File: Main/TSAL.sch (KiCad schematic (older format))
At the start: 39 parts, among them J1 Mini-SPOX, J2 Mini-SPOX, J3 Mini-Fit_Jr, J4 Mini-SPOX, J5 Mini-SPOX, Q1 IRLML2502, Q2 IRLML2502, Q3 IRLML2502, Q4 IRLML2502, U1 74HC08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

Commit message: Main board: Rev B schematics design
major redesign of power delivery and backup
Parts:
- removed C1, C4: 10u, Capacitor_SMD:C_0805_2012Metric_Pad1.15x1.40mm_HandSolder, symbol Device:C
- removed F1: 1A, Fuse:Fuseholder_Cylinder-5x20mm_Schurter_0031_8201_Horizontal_Open, symbol Device:Fuse
- removed R4: 1k, Resistor_SMD:R_0805_2012Metric_Pad1.15x1.40mm_HandSolder, symbol Device:R
- removed TP1: TP_Timer_En, TestPoint:TestPoint_THTPad_D2.0mm_Drill1.0mm, symbol Connector:TestPoint
- removed TP2: TP_RLED_Ctrl, TestPoint:TestPoint_THTPad_D2.0mm_Drill1.0mm, symbol Connector:TestPoint
- removed U3: TLV70033, Package_TO_SOT_SMD:SOT-23-5_HandSoldering, symbol Regulator_Linear:TLV70033_SOT23-5
- added Q5: IRLML2502, Package_TO_SOT_SMD:SOT-23, symbol Device:Q_NMOS_GSD
- C1: renamed from C2; value 100n -> 0.1uF; footprint Capacitor_SMD:C_0805_2012Metric_Pad1.15x1.40mm_HandSolder -> Capacitor_SMD:C_0402_1005Metric; Part CL21B104KACNNNC -> (none)
- C2: renamed from C3; value 100n -> 0.1uF; footprint Capacitor_SMD:C_0805_2012Metric_Pad1.15x1.40mm_HandSolder -> Capacitor_SMD:C_0402_1005Metric; Part CL21B104KACNNNC -> (none)
- C3: renamed from C5; value 100n -> 0.1uF; footprint Capacitor_SMD:C_0805_2012Metric_Pad1.15x1.40mm_HandSolder -> Capacitor_SMD:C_0402_1005Metric; symbol Device:C -> Device:C_Small; Part CL21B104KACNNNC -> (none)
- C4: renamed from C6; value 100n -> 0.1uF; footprint Capacitor_SMD:C_0805_2012Metric_Pad1.15x1.40mm_HandSolder -> Capacitor_SMD:C_0402_1005Metric; Part CL21B104KACNNNC -> (none)
- C5: renamed from C7; value 2.2u -> 2.2uF; footprint Capacitor_SMD:C_0805_2012Metric_Pad1.15x1.40mm_HandSolder -> Capacitor_SMD:C_0805_2012Metric; symbol Device:C -> Device:C_Small
- J1: renamed from J3; value Mini-Fit_Jr -> Micro-Fit; footprint Connector_Molex:Molex_Mini-Fit_Jr_5566-02A_2x01_P4.20mm_Vertical -> Connector_Molex:Molex_Micro-Fit_3.0_43045-0412_2x02_P3.00mm_Vertical; symbol Connector_Generic:Conn_01x02 -> Connector_Generic:Conn_02x02_Odd_Even; Part 39-28-1023 -> 43045-0413
- Q1: footprint Package_TO_SOT_SMD:SOT-23_Handsoldering -> Package_TO_SOT_SMD:SOT-23
- Q2: renamed from Q4; footprint Package_TO_SOT_SMD:SOT-23_Handsoldering -> Package_TO_SOT_SMD:SOT-23
- Q3: renamed from Q2; footprint Package_TO_SOT_SMD:SOT-23_Handsoldering -> Package_TO_SOT_SMD:SOT-23
- Q4: renamed from Q3; footprint Package_TO_SOT_SMD:SOT-23_Handsoldering -> Package_TO_SOT_SMD:SOT-23
- R1: footprint Resistor_SMD:R_0805_2012Metric_Pad1.15x1.40mm_HandSolder -> Resistor_SMD:R_0402_1005Metric; Part RC0805FR-07100KL -> (none)
- R10: renamed from R16; footprint Resistor_SMD:R_0805_2012Metric_Pad1.15x1.40mm_HandSolder -> Resistor_SMD:R_0402_1005Metric; Part RC0805FR-07100KL -> (none)
- R11: renamed from R15; footprint Resistor_SMD:R_0805_2012Metric_Pad1.15x1.40mm_HandSolder -> Resistor_SMD:R_0402_1005Metric; Part RC0805FR-07100KL -> (none)
- R2: renamed from R7; footprint Resistor_SMD:R_0805_2012Metric_Pad1.15x1.40mm_HandSolder -> Resistor_SMD:R_0402_1005Metric; symbol Device:R -> Device:R_Small; Part RC0805FR-07100KL -> (none)
- R3: renamed from R5; value 22k -> 10k; footprint Resistor_SMD:R_0805_2012Metric_Pad1.15x1.40mm_HandSolder -> Resistor_SMD:R_0805_2012Metric; symbol Device:R -> Device:R_Small; Part RC0805FR-0722KL -> (none)
- R4: renamed from R3; value 22k -> 10k; footprint Resistor_SMD:R_0805_2012Metric_Pad1.15x1.40mm_HandSolder -> Resistor_SMD:R_0402_1005Metric; symbol Device:R -> Device:R_Small; Part RC0805FR-0722KL -> (none)
- R5: renamed from R6; footprint Resistor_SMD:R_0805_2012Metric_Pad1.15x1.40mm_HandSolder -> Resistor_SMD:R_0805_2012Metric; symbol Device:R -> Device:R_Small; Part RC0805FR-07100KL -> (none)
- R6: renamed from R2; footprint Resistor_SMD:R_0805_2012Metric_Pad1.15x1.40mm_HandSolder -> Resistor_SMD:R_0402_1005Metric; Part RC0805FR-07100KL -> (none)
- R7: renamed from R19; footprint Resistor_SMD:R_0805_2012Metric_Pad1.15x1.40mm_HandSolder -> Resistor_SMD:R_0402_1005Metric; Part RC0805FR-07100KL -> (none)
- R8: renamed from R18; footprint Resistor_SMD:R_0805_2012Metric_Pad1.15x1.40mm_HandSolder -> Resistor_SMD:R_0402_1005Metric; Part RC0805FR-07100KL -> (none)
- R9: renamed from R17; footprint Resistor_SMD:R_0805_2012Metric_Pad1.15x1.40mm_HandSolder -> Resistor_SMD:R_0402_1005Metric; Part RC0805FR-07100KL -> (none)
- U1, U2: footprint Package_SO:SOIC-14_3.9x8.7mm_P1.27mm -> Package_SO:TSSOP-14_4.4x5mm_P0.65mm; Part SN74HC08DR -> SN74HC08PW
- U3: renamed from U4; footprint Package_SO:SOIC-8_3.9x4.9mm_P1.27mm -> Package_SO:TSSOP-8_3x3mm_P0.65mm; Part LMC555CMX -> LMC555CMM
- renumbered J1 to J2, J4 to J3, J2 to J4
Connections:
- net labels added: Dash_LED-, GNDPWR
- net labels removed: +2V5, TS_Inact_Out, VCC_F
- wire segments 91 -> 110
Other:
- note added: "AND Gates\nOnly light green light when all inputs are low\nOtherwise light blinking red light"
- note added: "Connectors"
- note added: "Double redundant AND gates and mosfets\nto comply with no single point of failure\nresulting in green light being lit requirement"
- note added: "High signals to indicate TS inactive\nTo comply with SCS short\nto ground detection requirement"
- note added: "Input from sense boards"
- note added: "Input pulldowns\nTo comply with SCS open circuit detection requirement"
- note added: "Ouput to LEDs"
- note added: "Power input 10-15V"
- note added: "Red light blink timer\n3Hz frequency\n52% duty cycle"
- note removed: "3Hz\n55% duty cycle"
- note removed: "High signals = TS inactive"
- moved on the sheet: C1, C2, C3, C4, C5, J2, J3, J4, J5, Q1, Q2, Q3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

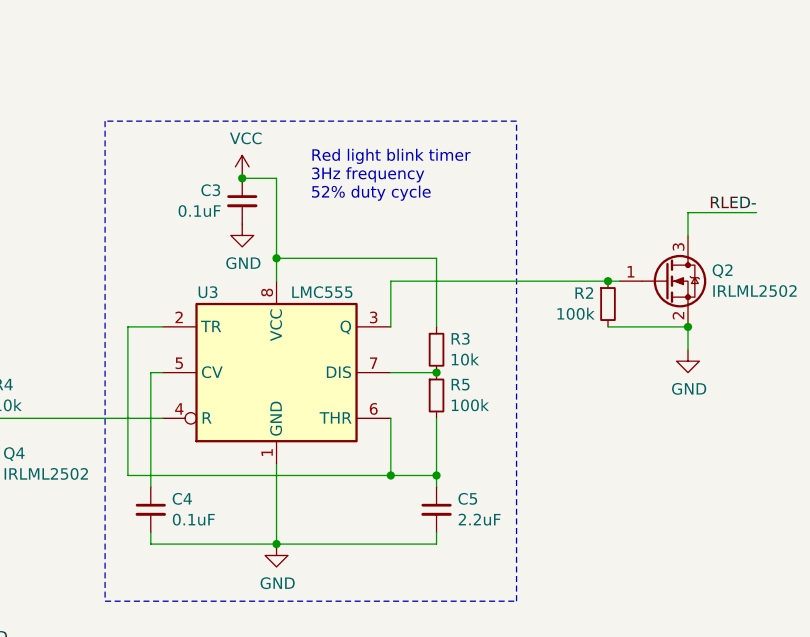
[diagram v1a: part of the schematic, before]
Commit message: Main board: final change to compensation network
None of this really matters with the supercaps at the output,
just trying to optimize the loop without them.
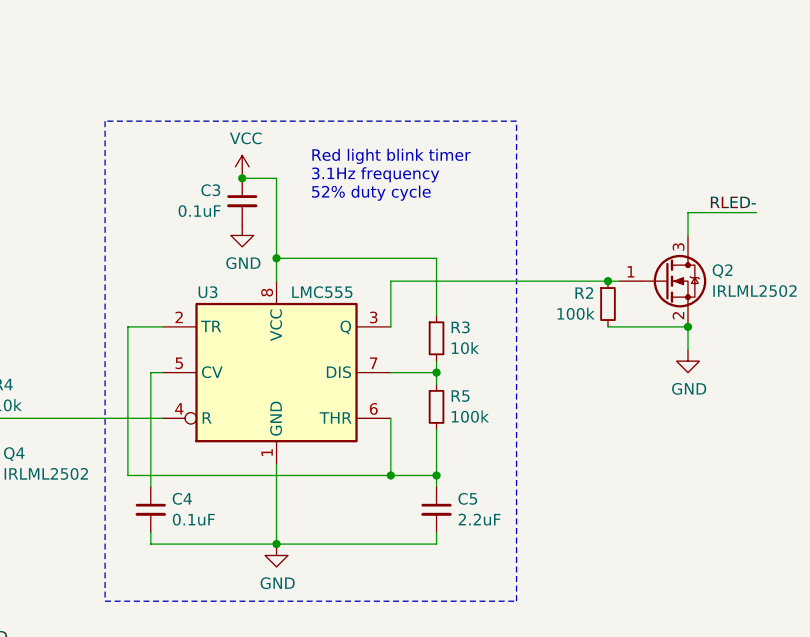
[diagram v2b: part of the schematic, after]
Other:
- note added: "Red light blink timer\n3.1Hz frequency\n52% duty cycle"
- note removed: "Red light blink timer\n3Hz frequency\n52% duty cycle"
- moved on the sheet: R3, R5
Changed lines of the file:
@@
 L Device:R_Small R3
 U 1 1 5DA7E3C4
-P 8500 4900
-F 0 "R3" H 8559 4946 50  0000 L CNN
-F 1 "10k" H 8559 4855 50  0000 L CNN
-F 2 "Resistor_SMD:R_0805_2012Metric" V 8430 4900 50  0001 C CNN
-F 3 "~" H 8500 4900 50  0001 C CNN
-F 4 "" H 8500 4900 50  0001 C CNN "Part"
-	1    8500 4900
+P 8500 4850
+F 0 "R3" H 8559 4896 50  0000 L CNN
+F 1 "10k" H 8559 4805 50  0000 L CNN
+F 2 "Resistor_SMD:R_0805_2012Metric" V 8430 4850 50  0001 C CNN
+F 3 "~" H 8500 4850 50  0001 C CNN
+F 4 "" H 8500 4850 50  0001 C CNN "Part"
+	1    8500 4850
 	1    0    0    -1
 $EndComp
@@
 L Device:R_Small R5
 U 1 1 5DA7E605
-P 8500 5100
-F 0 "R5" H 8559 5146 50  0000 L CNN
-F 1 "100k" H 8559 5055 50  0000 L CNN
-F 2 "Resistor_SMD:R_0805_2012Metric" V 8430 5100 50  0001 C CNN
-F 3 "~" H 8500 5100 50  0001 C CNN
-F 4 "" H 8500 5100 50  0001 C CNN "Part"
-	1    8500 5100
+P 8500 5150
+F 0 "R5" H 8559 5196 50  0000 L CNN
+F 1 "100k" H 8559 5105 50  0000 L CNN
+F 2 "Resistor_SMD:R_0805_2012Metric" V 8430 5150 50  0001 C CNN
+F 3 "~" H 8500 5150 50  0001 C CNN
+F 4 "" H 8500 5150 50  0001 C CNN "Part"
+	1    8500 5150
 	1    0    0    -1
 $EndComp
@@
 	1    0    0    -1
 $EndComp
-Text Notes 7950 4250 0    50   ~ 0
-Red light blink timer\n3Hz frequency\n52% duty cycle
 Wire Wire Line
 	7800 4500 7800 4600
@@
 Wire Wire Line
 	6200 6200 6200 6300
-Connection ~ 8500 5000
-Wire Wire Line
-	8500 5200 8500 5450
 Wire Wire Line
 	8500 5450 8300 5450
@@
 	8500 5750 8500 5700
 Wire Wire Line
-	8500 4500 8500 4800
+	8500 4500 8500 4750
 Wire Wire Line
 	7800 4150 7800 4500
@@
 Wire Wire Line
 	9250 4600 9300 4600
+Text Notes 7950 4250 0    50   ~ 0
+Red light blink timer\n3.1Hz frequency\n52% duty cycle
+Wire Wire Line
+	8500 5250 8500 5450
+Wire Wire Line
+	8500 5050 8500 5000
+Connection ~ 8500 5000
+Wire Wire Line
+	8500 5000 8500 4950
 $EndSCHEMATC

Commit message: Main: optimized layout
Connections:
- net GNDPWR is gone; now on net GND: J1.1 (Pin_1), J1.3 (Pin_3)
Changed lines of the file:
@@
 Wire Wire Line
 	6500 2000 6500 2050
-$Comp
-L power:GNDPWR #PWR03
-U 1 1 606A8035
-P 6500 2050
-F 0 "#PWR03" H 6500 1850 50  0001 C CNN
-F 1 "GNDPWR" H 6504 1896 50  0000 C CNN
-F 2 "" H 6500 2000 50  0001 C CNN
-F 3 "" H 6500 2000 50  0001 C CNN
-	1    6500 2050
-	1    0    0    -1
-$EndComp
 Wire Notes Line
 	7050 3900 7050 6000
@@
 Wire Wire Line
 	8500 5000 8500 4950
+$Comp
+L power:GND #PWR?
+U 1 1 60609209
+P 6500 2050
+AR Path="/5DE07D62/60609209" Ref="#PWR?"  Part="1"
+AR Path="/60609209" Ref="#PWR03"  Part="1"
+F 0 "#PWR03" H 6500 1800 50  0001 C CNN
+F 1 "GND" H 6505 1877 50  0000 C CNN
+F 2 "" H 6500 2050 50  0001 C CNN
+F 3 "" H 6500 2050 50  0001 C CNN
+	1    6500 2050
+	1    0    0    -1
+$EndComp
 $EndSCHEMATC

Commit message: Main: archive symbols and footprints
Kicad library management is really terrible.
This is pulled together with janky scripts and sed.
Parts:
- C1, C2: footprint Capacitor_SMD:C_0402_1005Metric -> archive:C_0402_1005Metric; symbol Device:C -> archive:Device_C
- C3, C4: footprint Capacitor_SMD:C_0402_1005Metric -> archive:C_0402_1005Metric; symbol Device:C_Small -> archive:Device_C_Small
- C5: footprint Capacitor_SMD:C_0805_2012Metric -> archive:C_0805_2012Metric; symbol Device:C_Small -> archive:Device_C_Small
- H1, H2, H3, H4: footprint MountingHole:MountingHole_3.2mm_M3_Pad -> archive:MountingHole_3.2mm_M3_Pad; symbol Mechanical:MountingHole -> archive:Mechanical_MountingHole
- J1: footprint Connector_Molex:Molex_Micro-Fit_3.0_43045-0412_2x02_P3.00mm_Vertical -> archive:Molex_Micro-Fit_3.0_43045-0412_2x02_P3.00mm_Vertical; symbol Connector_Generic:Conn_02x02_Odd_Even -> archive:Connector_Generic_Conn_02x02_Odd_Even
- J2: footprint Connector_Molex:Molex_SPOX_5267-03A_1x03_P2.50mm_Vertical -> archive:Molex_SPOX_5267-03A_1x03_P2.50mm_Vertical; symbol Connector_Generic:Conn_01x03 -> archive:Connector_Generic_Conn_01x03
- J3: footprint Connector_Molex:Molex_SPOX_5267-04A_1x04_P2.50mm_Vertical -> archive:Molex_SPOX_5267-04A_1x04_P2.50mm_Vertical; symbol Connector_Generic:Conn_01x04 -> archive:Connector_Generic_Conn_01x04
- J4: footprint Connector_Molex:Molex_SPOX_5267-06A_1x06_P2.50mm_Vertical -> archive:Molex_SPOX_5267-06A_1x06_P2.50mm_Vertical; symbol Connector_Generic:Conn_01x06 -> archive:Connector_Generic_Conn_01x06
- J5: footprint Connector_Molex:Molex_SPOX_5267-02A_1x02_P2.50mm_Vertical -> archive:Molex_SPOX_5267-02A_1x02_P2.50mm_Vertical; symbol Connector_Generic:Conn_01x02 -> archive:Connector_Generic_Conn_01x02
- Q1, Q2, Q3, Q4, Q5: footprint Package_TO_SOT_SMD:SOT-23 -> archive:SOT-23; symbol Device:Q_NMOS_GSD -> archive:Device_Q_NMOS_GSD
- R1, R6: footprint Resistor_SMD:R_0402_1005Metric -> archive:R_0402_1005Metric; symbol Device:R -> archive:Device_R
- R10, R11, R2, R4, R7, R8, R9: footprint Resistor_SMD:R_0402_1005Metric -> archive:R_0402_1005Metric; symbol Device:R_Small -> archive:Device_R_Small
- R3, R5: footprint Resistor_SMD:R_0805_2012Metric -> archive:R_0805_2012Metric; symbol Device:R_Small -> archive:Device_R_Small
- U1, U2: footprint Package_SO:TSSOP-14_4.4x5mm_P0.65mm -> archive:TSSOP-14_4.4x5mm_P0.65mm; symbol 74xx:74LS08 -> archive:74xx_74LS08
- U3: footprint Package_SO:TSSOP-8_3x3mm_P0.65mm -> archive:TSSOP-8_3x3mm_P0.65mm; symbol Timer:LM555xM -> archive:Timer_LM555xM

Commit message: Fixed LMC555 footprint error on main TSAL board
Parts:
- U3: footprint archive:TSSOP-8_3x3mm_P0.65mm -> Package_SO:VSSOP-8_3.0x3.0mm_P0.65mm
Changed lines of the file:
@@
 F 0 "U3" H 7500 5350 50  0000 C CNN
 F 1 "LMC555" H 8000 5350 50  0000 C CNN
-F 2 "archive:TSSOP-8_3x3mm_P0.65mm" H 7800 5000 50  0001 C CNN
+F 2 "Package_SO:VSSOP-8_3.0x3.0mm_P0.65mm" H 7800 5000 50  0001 C CNN
 F 3 "http://www.ti.com/lit/ds/symlink/lm555.pdf" H 7800 5000 50  0001 C CNN
 F 4 "LMC555CMM" H 7800 5000 50  0001 C CNN "Part"
